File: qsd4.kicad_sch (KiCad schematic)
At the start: 66 parts, among them J1 5-1814832-1, J2 5-1814832-1, J3 Conn_02x08_Odd_Even, J4 SJ-3524-SMT, U10 GALI-39, U3 SN74CBT3253, U4 SN74AC74PW, U5 AD8226ARZ-R7, U6 AD8226ARZ-R7, U7 AP2120N-2.5TRG1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

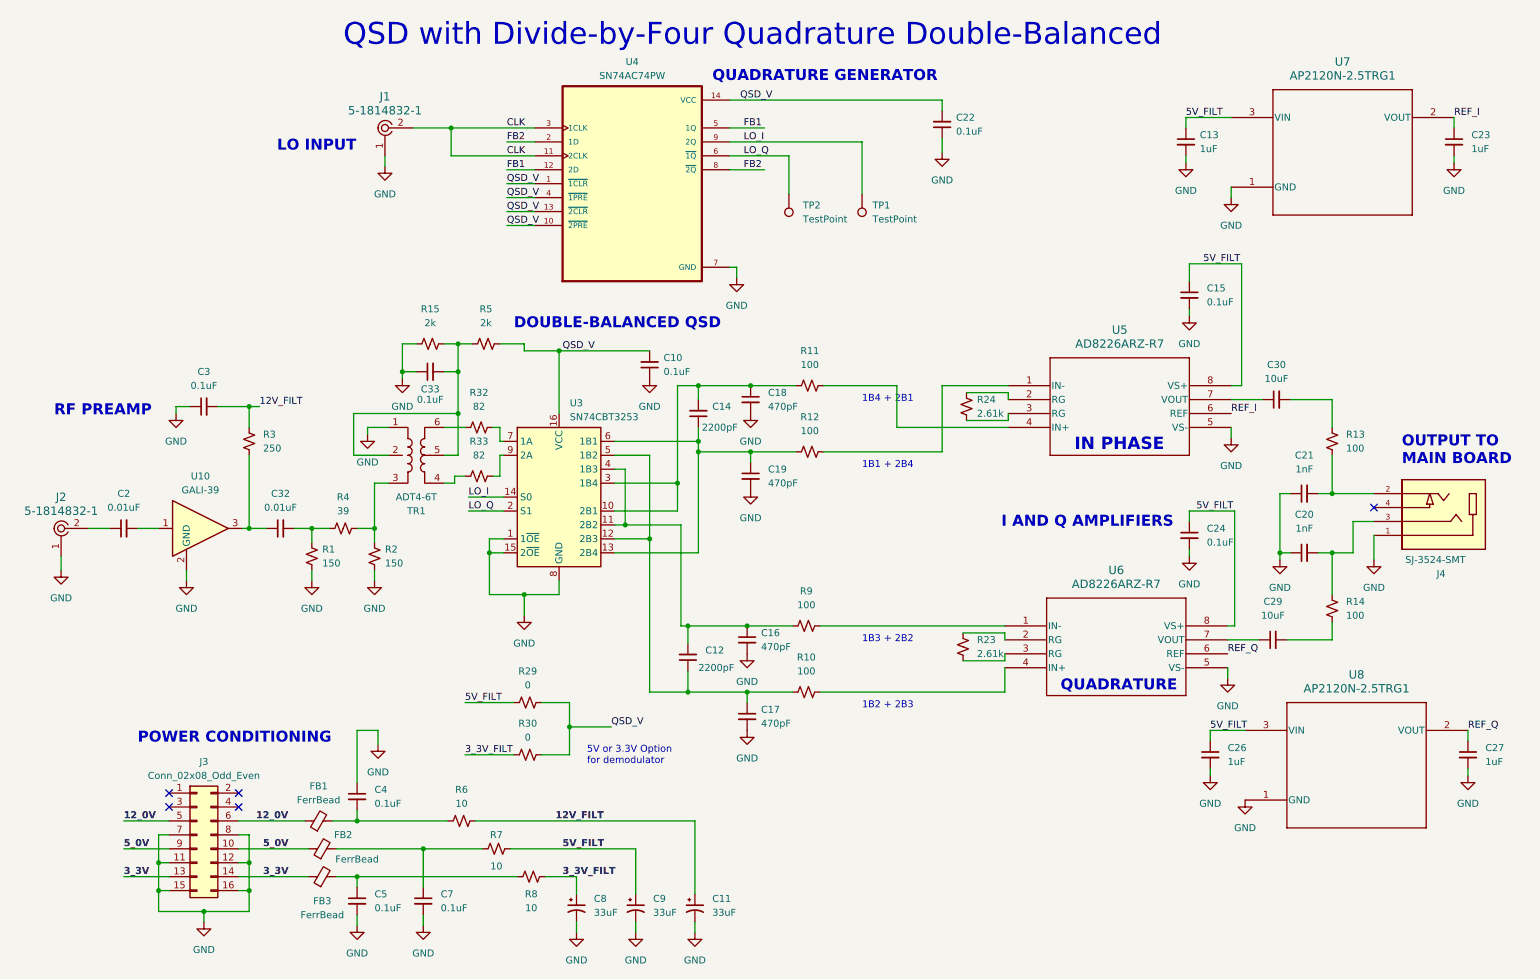
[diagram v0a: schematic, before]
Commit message: Version 1.1 PCB for the QSD4.  Documentation updated.
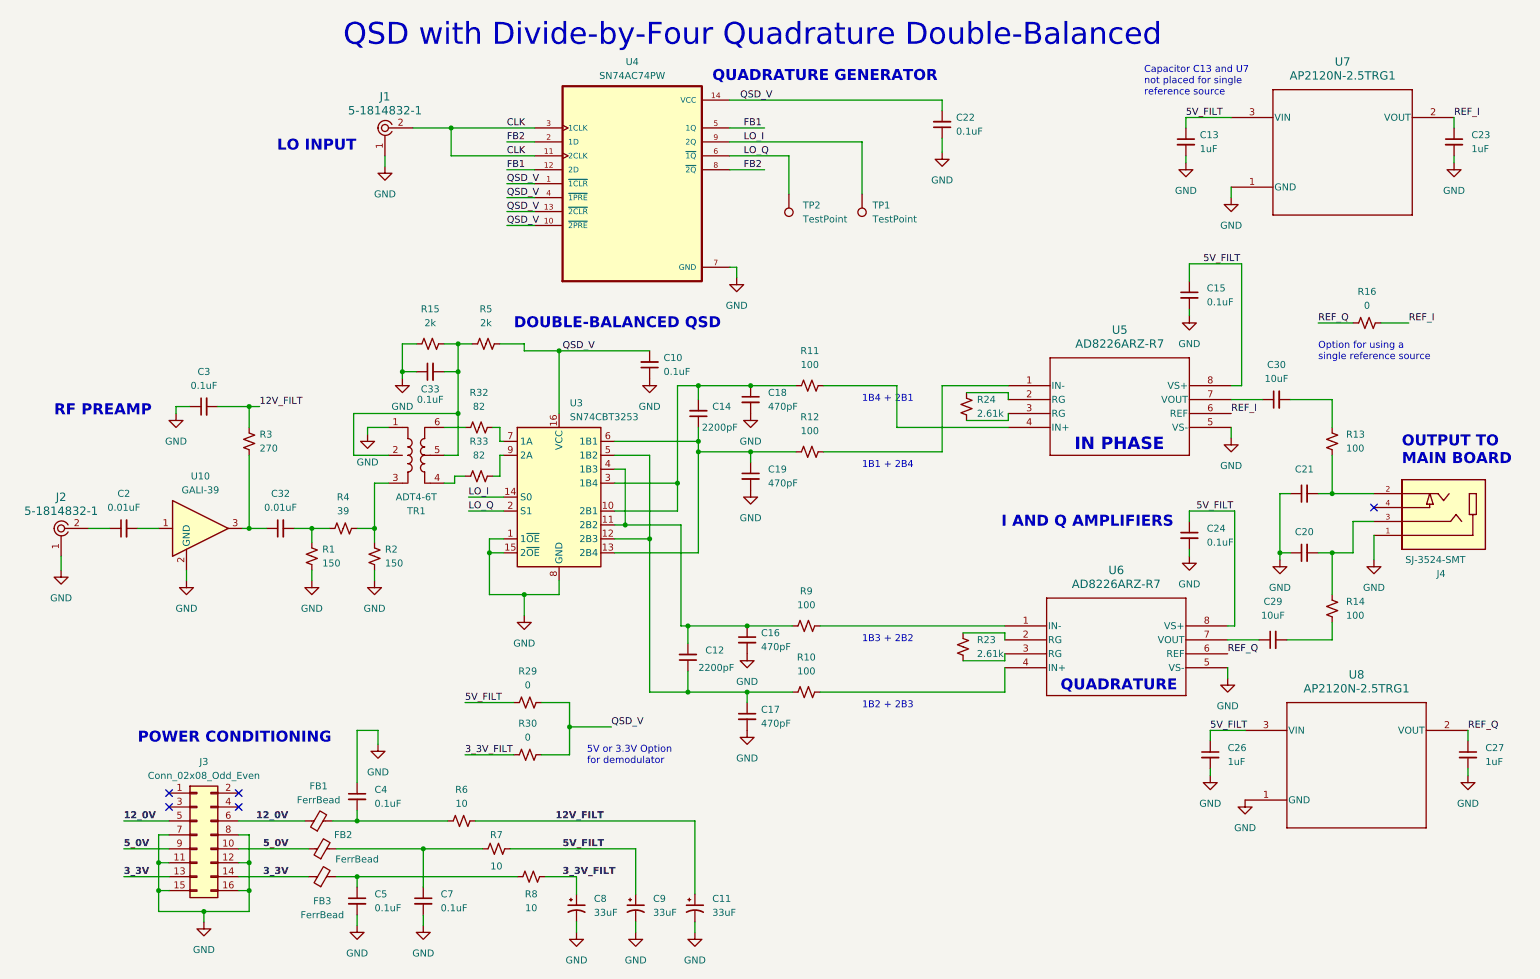
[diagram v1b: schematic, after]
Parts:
- added R16: 0, Resistor_SMD:R_1206_3216Metric, symbol Device:R_Small_US
- C20, C21: value 1nF -> ~
- R3: value 250 -> 270
- U3: footprint Package_SO:SSOP-16_4.4x5.2mm_P0.65mm -> Package_SO:TSSOP-16_4.4x5mm_P0.65mm
- U4: footprint SN74AC74PW:SOP65P640X120-14N -> Package_SO:TSSOP-14_4.4x5mm_P0.65mm
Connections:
- net REF_I: now also R16.2
- net REF_Q: now also R16.1
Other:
- note added: "Capacitor C13 and U7 not placed for single reference source"
- note added: "Option for using a single reference source"
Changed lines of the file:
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@@
   (title_block
     (title "QSD4 with Divide-by-Four Quadrature Double-Balanced")
-    (date "2023-10-26")
+    (date "2023-11-17")
     (rev "1.0")
   )
@@
     (stroke (width 0) (type default))
   )
+  (wire (pts (xy 250.19 72.39) (xy 256.54 72.39))
+    (stroke (width 0) (type default))
+  )
   (wire (pts (xy 135.255 139.7) (xy 146.05 139.7))
     (stroke (width 0) (type default))
@@
     (stroke (width 0) (type default))
   )
+  (wire (pts (xy 261.62 72.39) (xy 266.7 72.39))
+    (stroke (width 0) (type default))
+  )
   (wire (pts (xy 252.73 96.52) (xy 252.73 103.505))
     (stroke (width 0) (type default))
@@
     (effects (font (size 2 2) bold) (justify left bottom))
   )
+  (text "Option for using a\nsingle reference source" (at 250.19 79.375 0)
+    (effects (font (size 1.27 1.27)) (justify left bottom))
+  )
   (text "POWER CONDITIONING" (at 34.925 149.225 0)
     (effects (font (size 2 2) bold) (justify left bottom))
@@
     (effects (font (size 1.27 1.27)) (justify left bottom))
   )
+  (text "Capacitor C13 and U7\nnot placed for single\nreference source"
+    (at 218.44 31.115 0)
+    (effects (font (size 1.27 1.27)) (justify left bottom))
+  )
   (text "QSD with Divide-by-Four Quadrature Double-Balanced"
     (at 72.39 22.225 0)
@@
     (effects (font (size 1.27 1.27)) (justify left bottom))
   )
+  (label "REF_Q" (at 250.19 72.39 0) (fields_autoplaced)
+    (effects (font (size 1.27 1.27)) (justify left bottom))
+  )
   (label "3_3V" (at 32.385 173.355 0) (fields_autoplaced)
     (effects (font (size 1.27 1.27) bold) (justify left bottom))
@@
     (effects (font (size 1.27 1.27)) (justify left bottom))
   )
+  (label "REF_I" (at 266.7 72.39 0) (fields_autoplaced)
+    (effects (font (size 1.27 1.27)) (justify left bottom))
+  )
   (label "3_3V_FILT" (at 94.615 151.13 0) (fields_autoplaced)
     (effects (font (size 1.27 1.27)) (justify left bottom))
@@
       (effects (font (size 1.27 1.27)))
     )
-    (property "Footprint" "SN74AC74PW:SOP65P640X120-14N" (at 125.095 46.99 0)
+    (property "Footprint" "Package_SO:TSSOP-14_4.4x5mm_P0.65mm" (at 125.095 46.99 0)
       (effects (font (size 1.27 1.27)) (justify bottom) hide)
     )
@@
   (symbol (lib_id "Device:R_Small_US") (at 55.245 93.98 0) (unit 1)
     (in_bom yes) (on_board yes) (dnp no) (fields_autoplaced)
-    (property "Reference" "R3" (at 57.785 92.71 0)
+    (property "Reference" "R3" (at 57.15 92.71 0)
       (effects (font (size 1.27 1.27)) (justify left))
     )
-    (property "Value" "250" (at 57.785 95.25 0)
+    (property "Value" "270" (at 57.15 95.25 0)
       (effects (font (size 1.27 1.27)) (justify left))
     )
@@
     )
   )
+  (symbol (lib_id "Device:R_Small_US") (at 259.08 72.39 90) (unit 1)
+    (in_bom yes) (on_board yes) (dnp no) (fields_autoplaced)
+    (property "Reference" "R16" (at 259.08 66.675 90)
+      (effects (font (size 1.27 1.27)))
+    )
+    (property "Value" "0" (at 259.08 69.215 90)
+      (effects (font (size 1.27 1.27)))
+    )
+    (property "Footprint" "Resistor_SMD:R_1206_3216Metric" (at 259.08 72.39 0)
+      (effects (font (size 1.27 1.27)) hide)
+    )
+    (property "Datasheet" "~" (at 259.08 72.39 0)
+      (effects (font (size 1.27 1.27)) hide)
+    )
+    (pin "1")
+    (pin "2")
+    (instances
+      (project "qsd4"
+        (path "/e85a7744-7948-44f7-b41f-dd9b75249984"
+          (reference "R16") (unit 1)
+        )
+      )
+    )
+  )
   (symbol (lib_id "Device:R_Small_US") (at 186.055 87.63 0) (unit 1)
     (in_bom yes) (on_board yes) (dnp no) (fields_autoplaced)
@@
   (symbol (lib_id "Device:C_Small") (at 247.65 114.3 90) (unit 1)
     (in_bom yes) (on_board yes) (dnp no) (fields_autoplaced)
-    (property "Reference" "C20" (at 247.6563 107.315 90)
+    (property "Reference" "C20" (at 247.6563 110.49 90)
       (effects (font (size 1.27 1.27)))
     )
-    (property "Value" "1nF" (at 247.6563 109.855 90)
+    (property "Value" "~" (at 247.6563 109.855 90)
       (effects (font (size 1.27 1.27)))
     )
@@
       (effects (font (size 1.27 1.27)) (justify left))
     )
-    (property "Footprint" "Package_SO:SSOP-16_4.4x5.2mm_P0.65mm" (at 111.76 104.14 0)
+    (property "Footprint" "Package_SO:TSSOP-16_4.4x5mm_P0.65mm" (at 111.76 104.14 0)
       (effects (font (size 1.27 1.27)) hide)
     )
@@
   (symbol (lib_id "Device:C_Small") (at 247.65 103.505 90) (unit 1)
     (in_bom yes) (on_board yes) (dnp no) (fields_autoplaced)
-    (property "Reference" "C21" (at 247.6563 96.52 90)
+    (property "Reference" "C21" (at 247.6563 99.06 90)
       (effects (font (size 1.27 1.27)))
     )
-    (property "Value" "1nF" (at 247.6563 99.06 90)
+    (property "Value" "~" (at 247.6563 99.06 90)
       (effects (font (size 1.27 1.27)))
     )
